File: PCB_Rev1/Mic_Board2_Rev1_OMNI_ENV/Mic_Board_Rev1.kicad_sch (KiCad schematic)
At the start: 26 parts, among them J1 Conn_01x03_Pin, J71 532610771, U1 OPA1671IDBVR

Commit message: Micboard Omni PCB
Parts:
- renumbered J71 to J2
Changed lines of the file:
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@@
 	(wire
 		(pts
+			(xy 236.22 96.52) (xy 236.22 97.79)
+		)
+		(stroke
+			(width 0)
+			(type default)
+		)
+	)
+	(wire
+		(pts
 			(xy 151.13 92.71) (xy 162.56 92.71)
 		)
@@
 	(wire
 		(pts
+			(xy 236.22 91.44) (xy 236.22 92.71)
+		)
+		(stroke
+			(width 0)
+			(type default)
+		)
+	)
+	(wire
+		(pts
 			(xy 248.92 120.65) (xy 243.84 120.65)
 		)
@@
 	(wire
 		(pts
+			(xy 236.22 93.98) (xy 236.22 95.25)
+		)
+		(stroke
+			(width 0)
+			(type default)
+		)
+	)
+	(wire
+		(pts
 			(xy 78.74 128.27) (xy 87.63 128.27)
 		)
@@
 		(on_board yes)
 		(dnp no)
-		(property "Reference" "J71"
+		(property "Reference" "J2"
 			(at 270.51 110.49 0)
 			(effects
@@
 			(project "Mic_Board_Rev1"
 				(path "/7002bcc8-d574-4d7e-a21f-bd05f0fc5ee4"
-					(reference "J71")
+					(reference "J2")
 					(unit 1)
 				)
@@
 	(symbol
 		(lib_id "Connector:Conn_01x03_Pin")
-		(at 241.3 95.25 180)
+		(at 241.3 93.98 180)
 		(unit 1)
 		(exclude_from_sim no)
@@
 		(dnp no)
 		(property "Reference" "J1"
-			(at 254 93.98 0)
+			(at 254 92.71 0)
 			(effects
 				(font
@@
 				)
 				(justify right)
-				(hide yes)
 			)
 		)
 		(property "Value" "Conn_01x03_Pin"
-			(at 254 96.52 0)
+			(at 254 95.25 0)
 			(effects
 				(font
@@
 				)
 				(justify right)
-				(hide yes)
 			)
 		)
 		(property "Footprint" "Connector_PinHeader_2.54mm:PinHeader_1x03_P2.54mm_Vertical"
-			(at 241.3 95.25 0)
+			(at 241.3 93.98 0)
 			(effects
 				(font
@@
 		)
 		(property "Datasheet" "~"
-			(at 241.3 95.25 0)
+			(at 241.3 93.98 0)
 			(effects
 				(font
@@
 		)
 		(property "Description" ""
-			(at 241.3 95.25 0)
+			(at 241.3 93.98 0)
 			(effects
 				(font

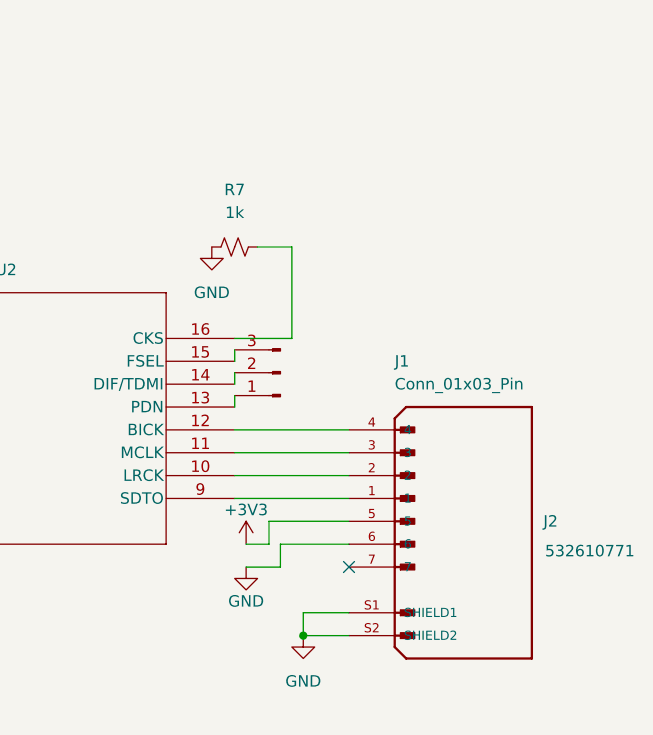
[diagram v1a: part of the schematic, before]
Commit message: connections for gpio and micboards
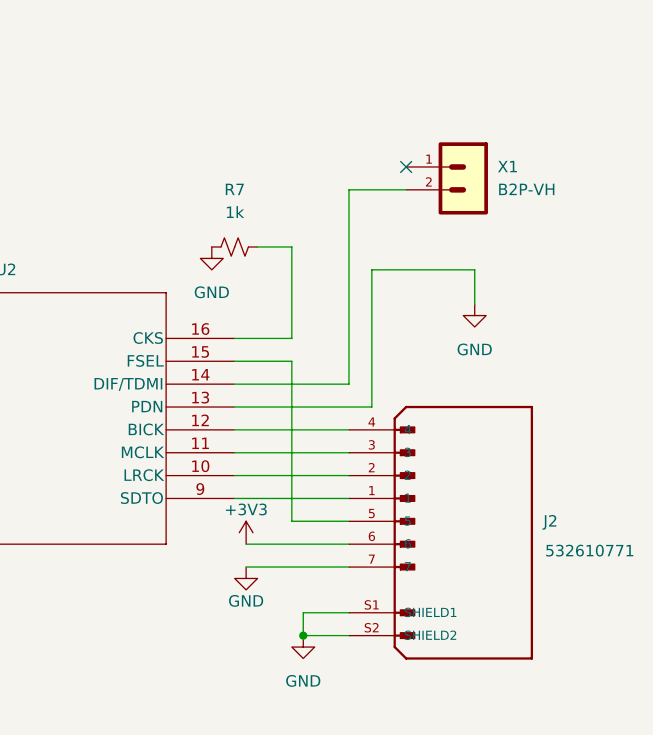
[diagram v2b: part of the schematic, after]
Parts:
- removed J1: Conn_01x03_Pin, Connector_PinHeader_2.54mm:PinHeader_1x03_P2.54mm_Vertical, symbol Connector:Conn_01x03_Pin
- added X1: B2P-VH, Footprints:B2P-VH, symbol B2P-VH:B2P-VH
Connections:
- net +3V3: now also J2.6; no longer J2.5
- net GND: now also J2.7, U2.13 (PDN); no longer J2.6
- net at U2.14 (DIF/TDMI): now also X1.2
- net at U2.15 (FSEL): now also J2.5
